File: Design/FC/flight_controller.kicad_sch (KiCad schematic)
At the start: 1 part, among them U1 STM32H747BIT6

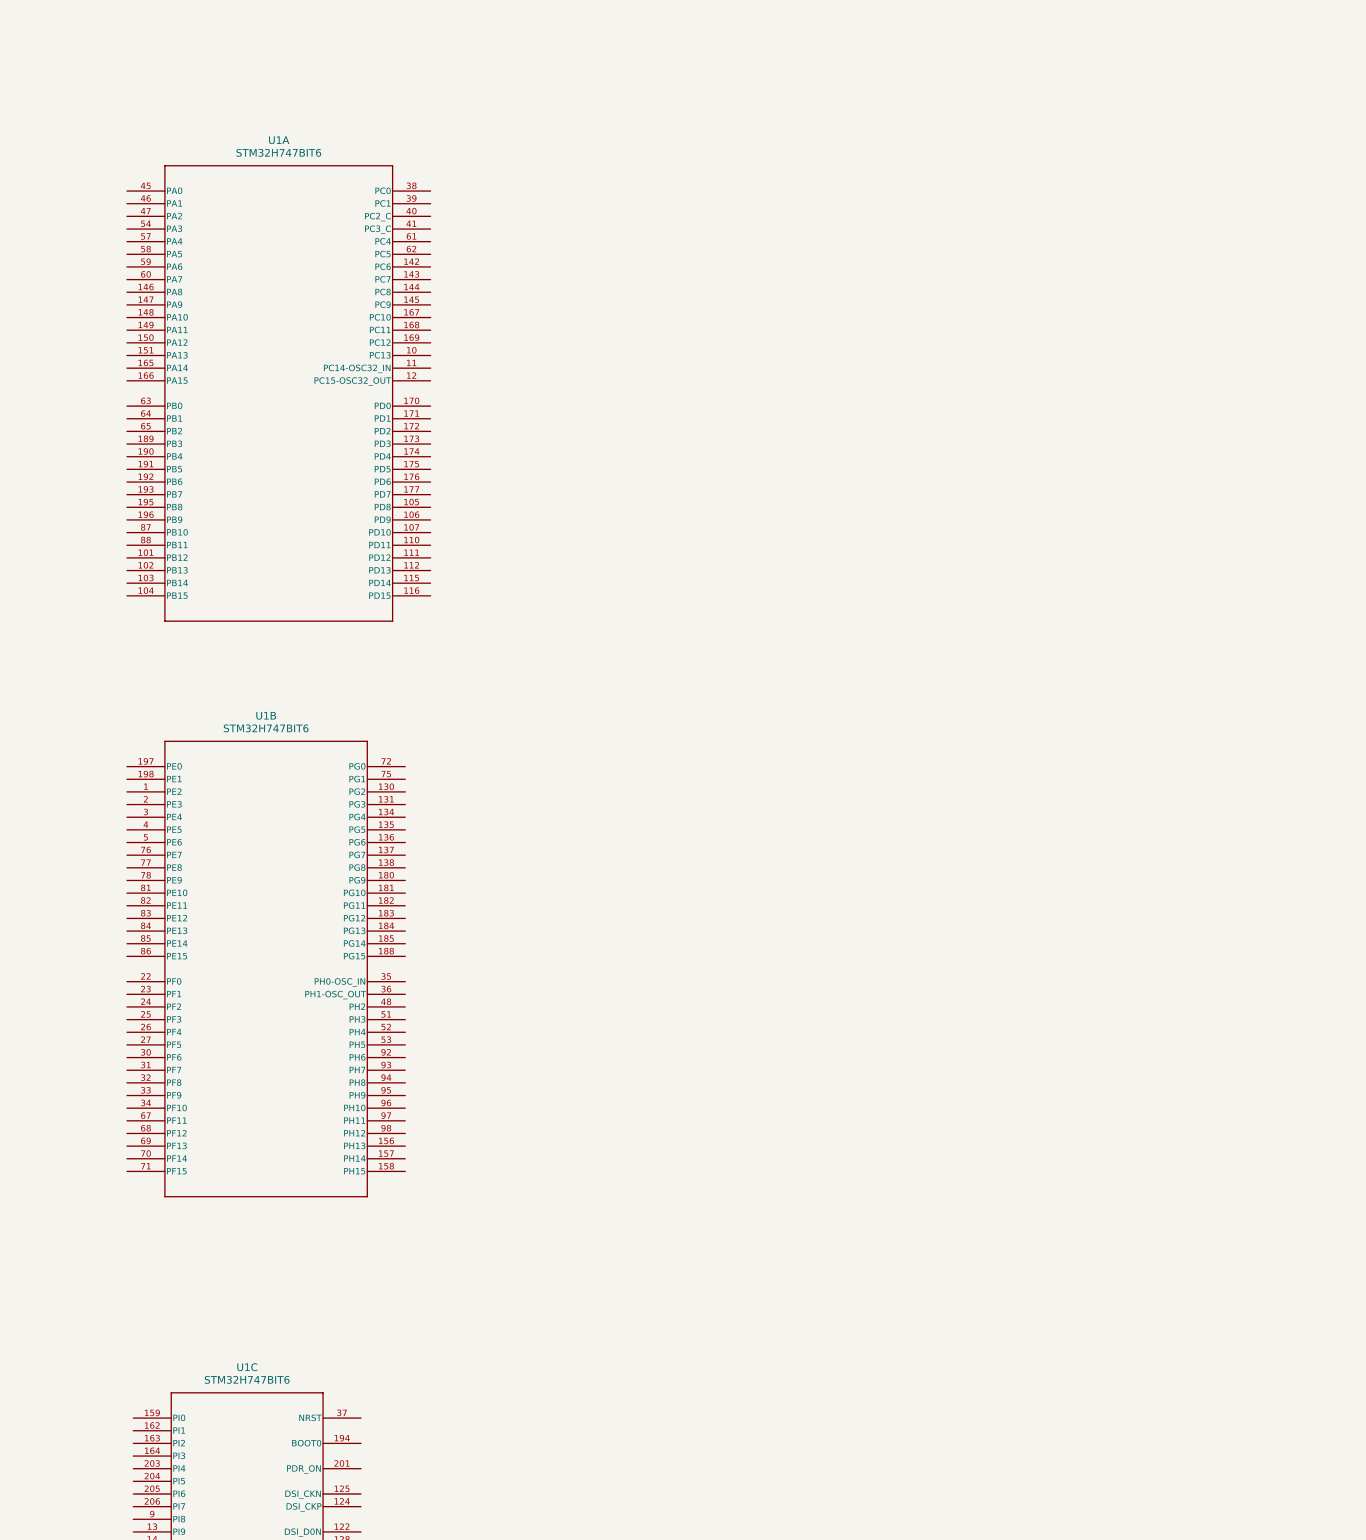
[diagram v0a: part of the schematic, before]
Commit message: started on swd interface
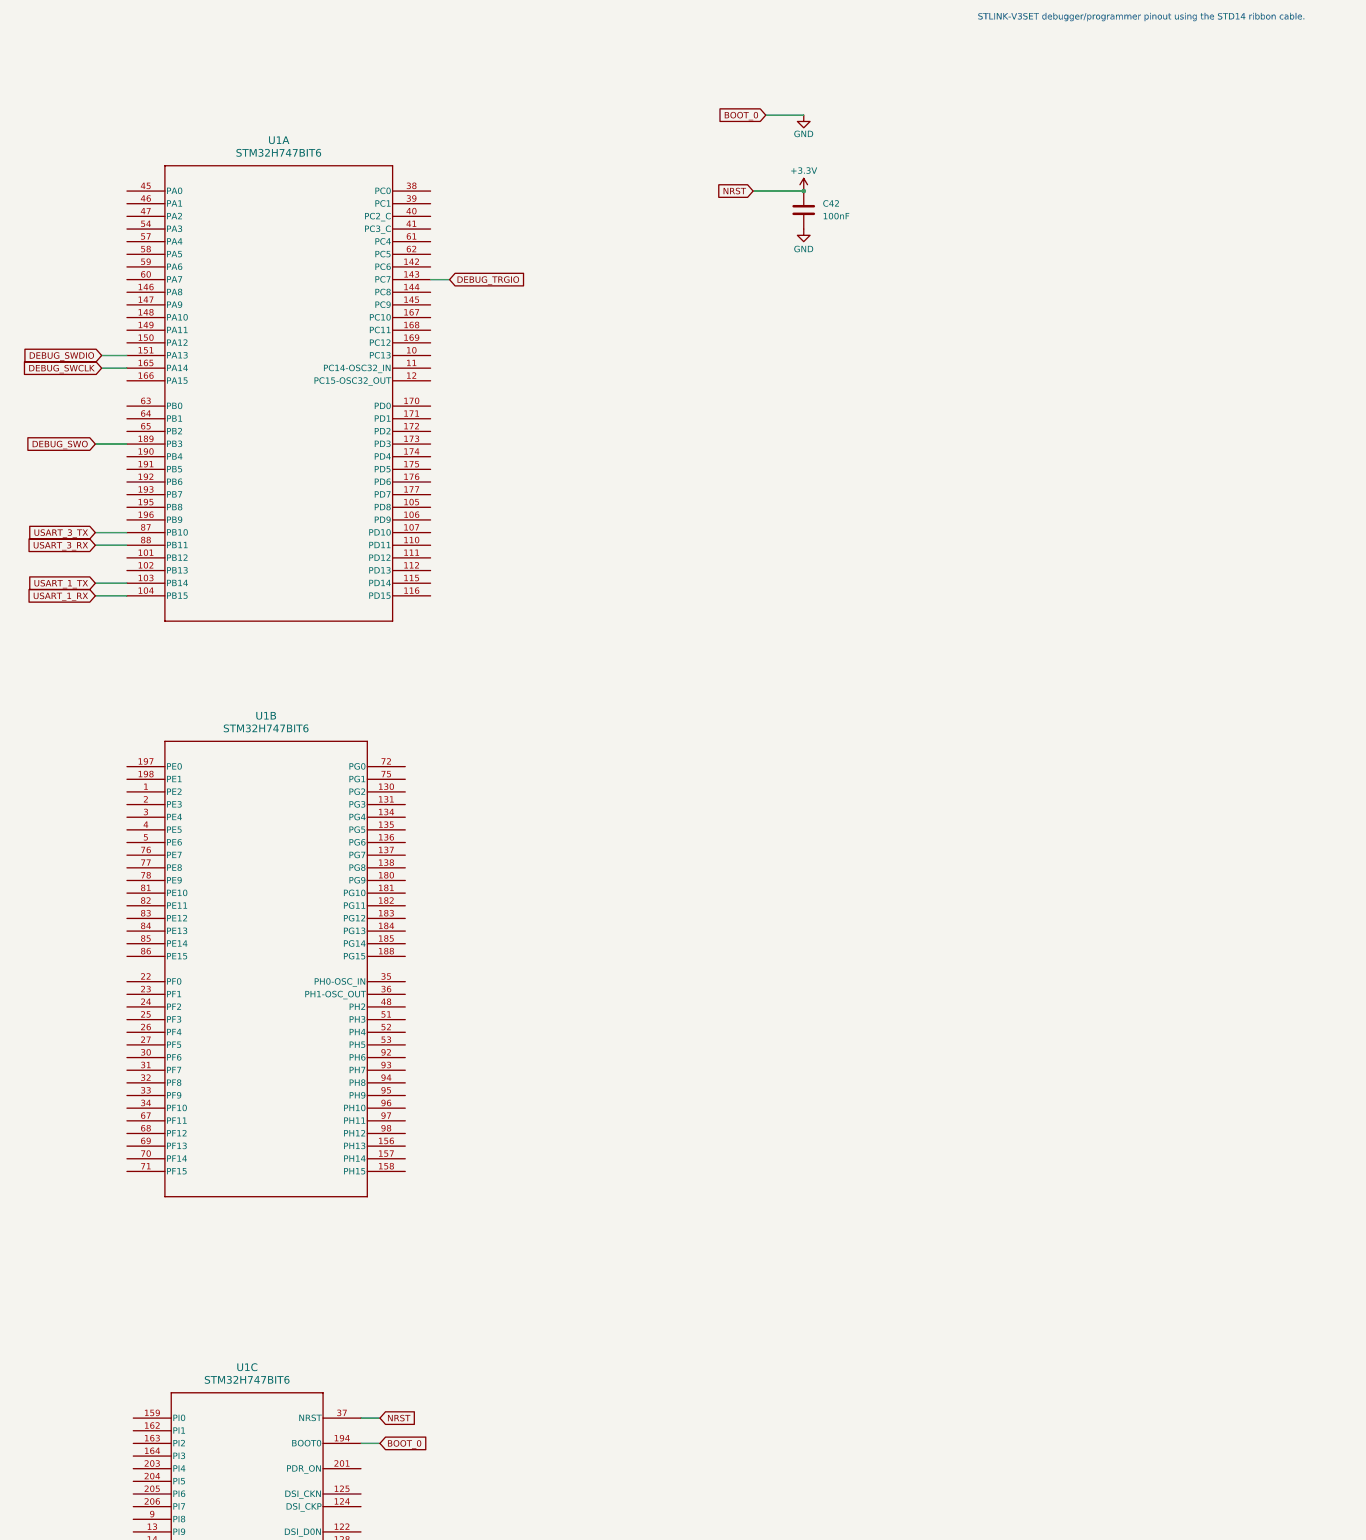
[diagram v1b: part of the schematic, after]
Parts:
- added C42: 100nF, symbol Device:C
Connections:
- net USART_1_TX: now reaches U1.103 (PB14)
- net USART_1_RX: now reaches U1.104 (PB15)
- net DEBUG_TRGIO: now reaches U1.143 (PC7)
- net DEBUG_SWDIO: now reaches U1.151 (PA13)
- net DEBUG_SWCLK: now reaches U1.165 (PA14)
- net DEBUG_SWO: now reaches U1.189 (PB3)
- net USART_3_TX: now reaches U1.87 (PB10)
- net USART_3_RX: now reaches U1.88 (PB11)
- net GND: now reaches U1.194 (BOOT0)
- net GND: now also C42.2
- net +3.3V: now reaches U1.37 (NRST)
- net +3.3V: now also C42.1
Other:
- note added: "STLINK-V3SET debugger/programmer pinout using the STD14 ribbon cable."

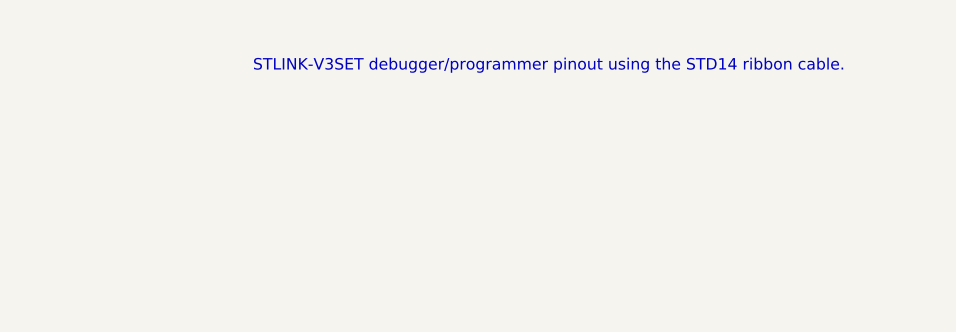
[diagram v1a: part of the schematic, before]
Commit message: crlf vs lf for kicad
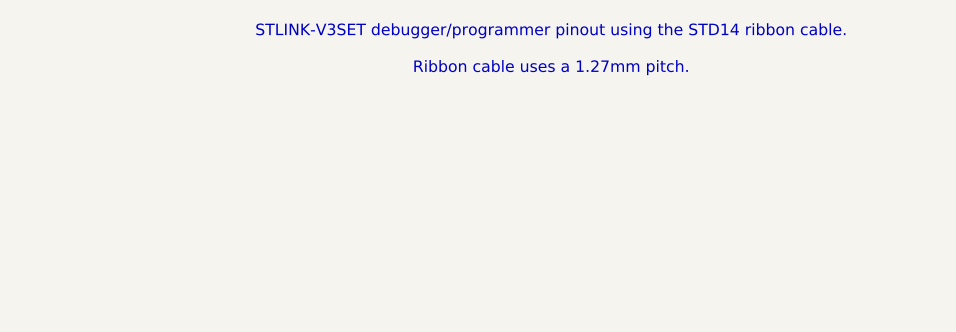
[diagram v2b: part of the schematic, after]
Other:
- note added: "STLINK-V3SET debugger/programmer pinout using the STD14 ribbon cable. Ribbon cable uses a 1.27mm pitch."
- note removed: "STLINK-V3SET debugger/programmer pinout using the STD14 ribbon cable."
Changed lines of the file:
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@@
 	(generator_version "9.0")
 	(paper "C")
-	(text "STLINK-V3SET debugger/programmer pinout using the STD14 ribbon cable."
+	(text "STLINK-V3SET debugger/programmer pinout using the STD14 ribbon cable.\n\nRibbon cable uses a 1.27mm pitch."
 		(exclude_from_sim no)
-		(at 249.428 23.622 0)
+		(at 249.682 21.844 0)
 		(effects
 			(font

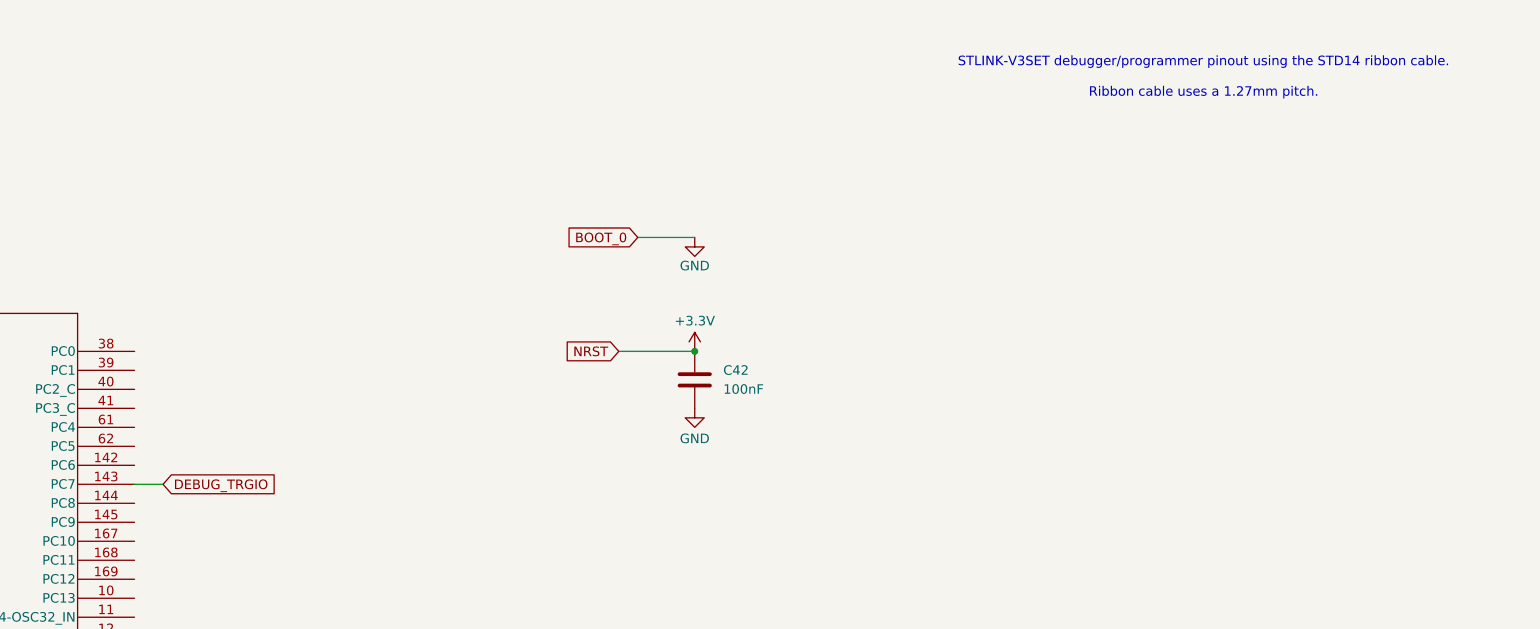
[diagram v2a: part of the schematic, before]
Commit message: added debug connector
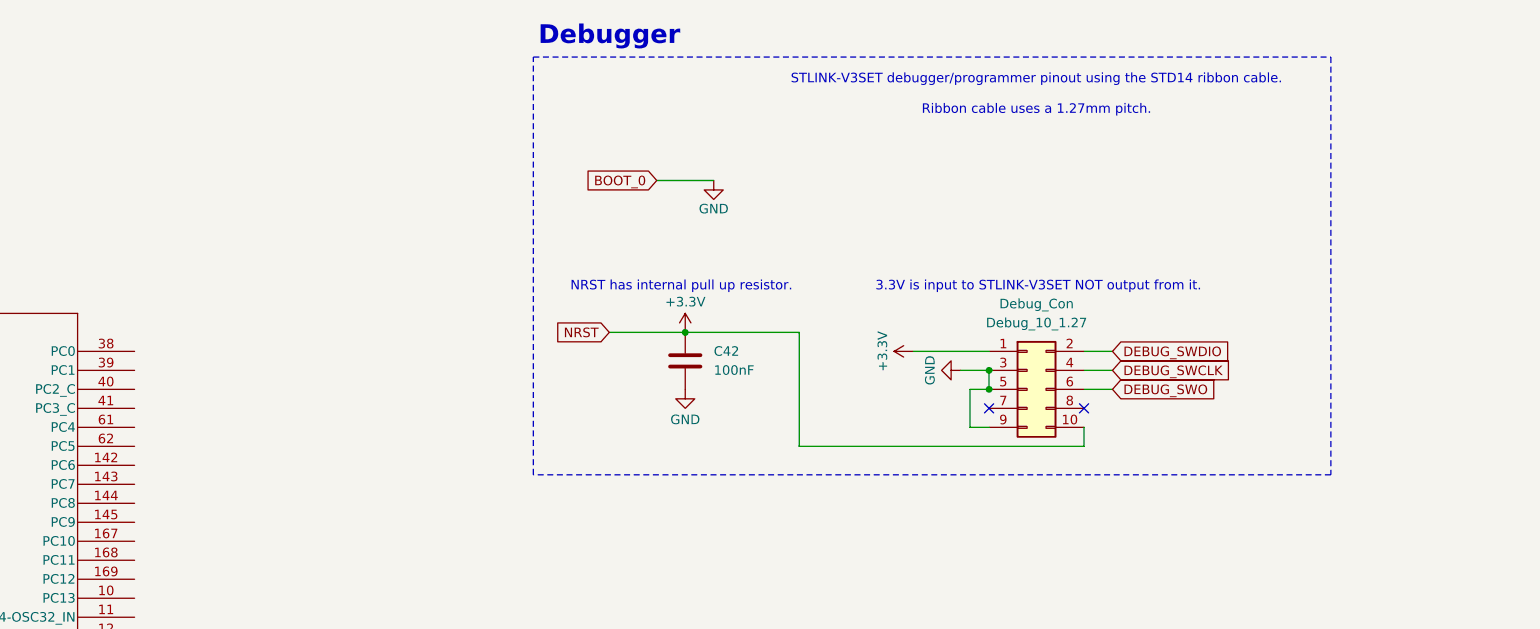
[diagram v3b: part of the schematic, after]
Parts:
- added Debug_Con: Debug_10_1.27, symbol Connector_Generic:Conn_02x05_Odd_Even
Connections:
- net +3.3V: now also Debug_Con.1 (Pin_1), Debug_Con.10 (Pin_10)
- net DEBUG_SWCLK: now also Debug_Con.4 (Pin_4)
- net DEBUG_SWDIO: now also Debug_Con.2 (Pin_2)
- net DEBUG_SWO: now also Debug_Con.6 (Pin_6)
- net GND: now also Debug_Con.3 (Pin_3), Debug_Con.5 (Pin_5), Debug_Con.9 (Pin_9)
- net DEBUG_TRGIO: no longer names the net of U1.143 (PC7)
- no-connect marks 0 -> 2
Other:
- note added: "3.3V is input to STLINK-V3SET NOT output from it."
- note added: "Debugger"
- note added: "NRST has internal pull up resistor."
- moved on the sheet: C42
